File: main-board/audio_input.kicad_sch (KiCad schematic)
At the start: 46 parts, among them J4 NCJ6FA-H-0, J6 NCJ6FA-H-0, Q1 MMBT3904, Q2 MMBT3906, Q3 MMBT3906, Q4 MMBT3904, U4 THAT1246, U5 THAT1246, U6 OPA1656ID, U7 LM2903

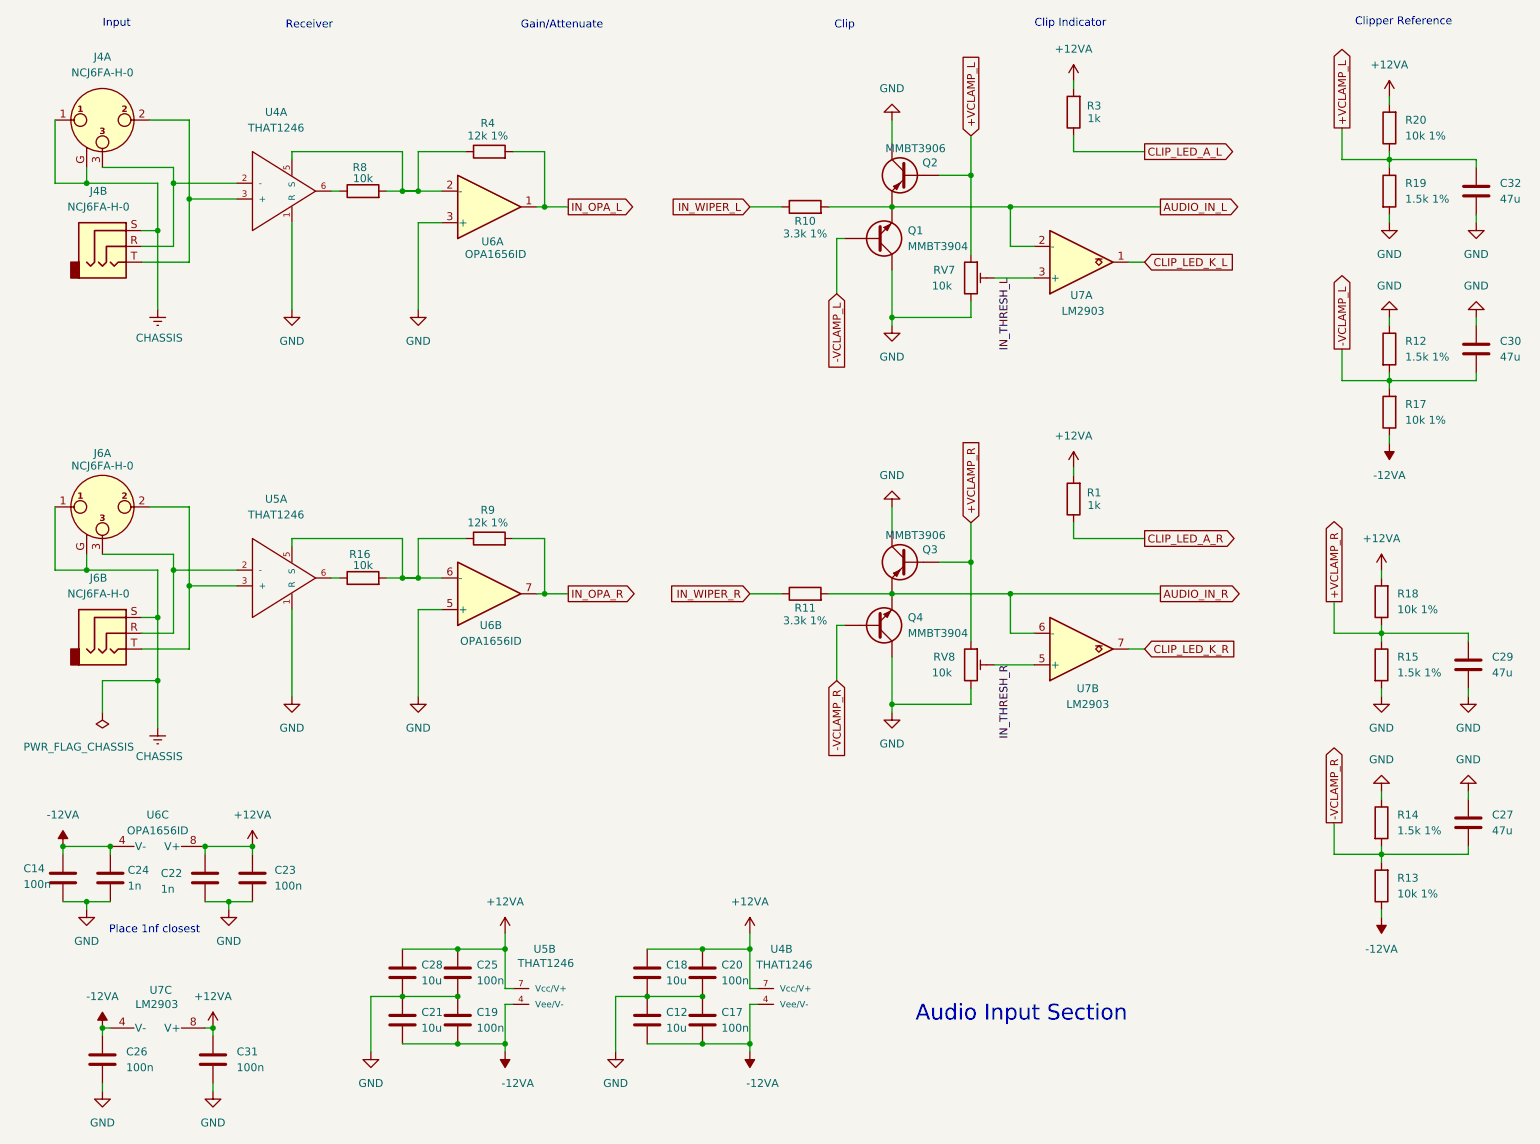
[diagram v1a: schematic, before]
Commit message: Tackle pre expermintal work (#28)
**Pre-experimental fixes — #18 #19 #20 #21**

Four correctness fixes on the input clamp circuit before the next experimental round:

- **Clamp transistor footprint** (#18): Switched Q_clamp from TO-92 (2N3906) to SOT-23 (PZT3906) — updates datasheet, description, sim pin mapping (B/E/C), and footprint filter in the PCB.
- **Threshold trimmer value** (#19): Raised RV_threshold from 10k → 100k so the wiper no longer drags down the clamp reference positive rail.
- **Sense line placement notes** (#20): Added schematic annotations directing R8 and R16 close to U6b to keep the sense lines short; corrected junction positions in the output topology section.
- **RV8/RV7 swap and labels** (#21): Swapped the two trimmers and added labels so they place cleanly on the PCB.

No functional changes to signal path topology — all changes are component selection, value correction, placement guidance, or layout clarity.

* swap and label rv8/7 so they lay out clearly - fixes #21
* fix sense error for output topology - fixes #20
* make threshold trimmer 100k so it doesn't drag down the clamp ref +ve rail - fixes #19
* fix footprint on the clamp transistors - fixes #18
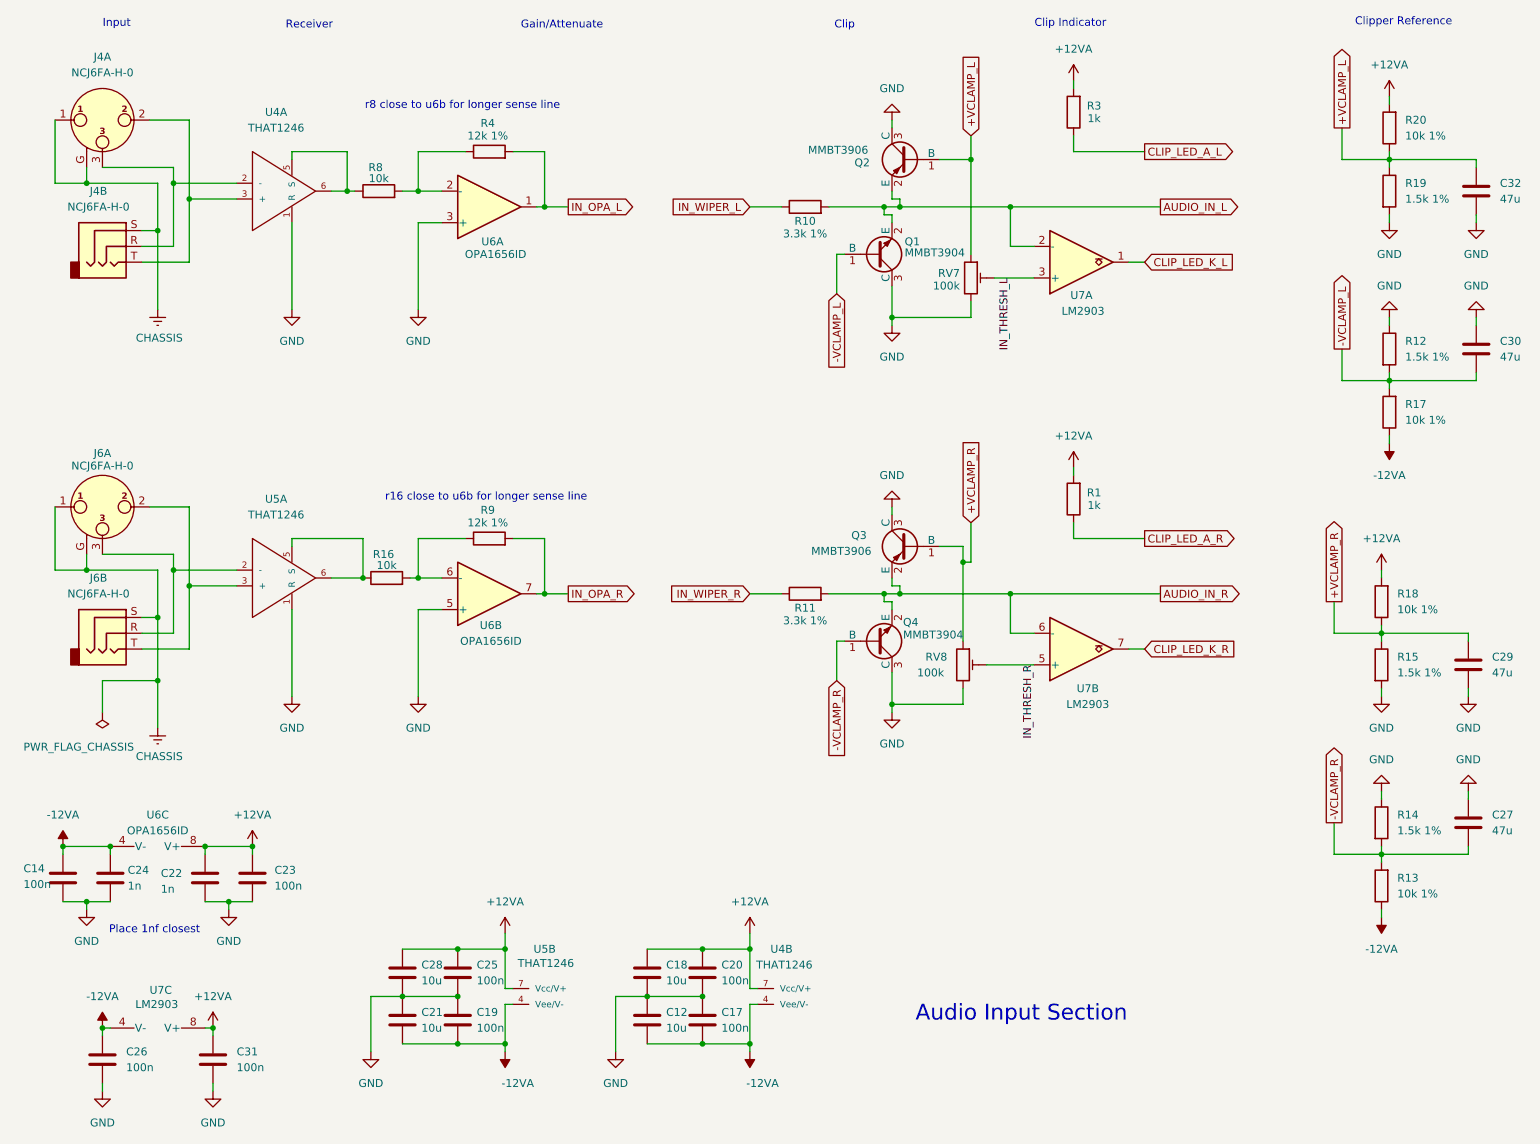
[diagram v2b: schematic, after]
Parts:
- Q1, Q4: symbol Transistor_BJT:2N3904 -> Transistor_BJT:MMBT3904
- Q2, Q3: symbol Transistor_BJT:2N3906 -> Transistor_BJT:MMBT3906
- RV7: value 10k -> 100k; Label (none) -> ICT_L
- RV8: value 10k -> 100k; Label (none) -> ICT_R
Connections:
- net +VCLAMP_L: now also Q2.1 (B); no longer Q2.2 (B)
- net +VCLAMP_R: now also Q3.1 (B); no longer Q3.2 (B)
- net -VCLAMP_L: now also Q1.1 (B); no longer Q1.2 (B)
- net -VCLAMP_R: now also Q4.1 (B); no longer Q4.2 (B)
- net AUDIO_IN_L: now also Q1.2 (E), Q2.2 (E); no longer Q1.1 (E), Q2.1 (E)
- net AUDIO_IN_R: now also Q3.2 (E), Q4.2 (E); no longer Q3.1 (E), Q4.1 (E)
- net at R16.2, R9.1, U6.6 (-): no longer U5.5 (S)
- net at R4.1, R8.2, U6.2 (-): no longer U4.5 (S)
- net at R8.1, U4.6: now also U4.5 (S)
- net at R16.1, U5.6: now also U5.5 (S)
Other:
- note added: "r16 close to u6b for longer sense line"
- note added: "r8 close to u6b for longer sense line"
- moved on the sheet: R16, R8, RV8
